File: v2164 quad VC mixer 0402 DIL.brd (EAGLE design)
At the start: 31.8 x 14 mm, 34 parts, among them IC1 TL072JD, Q1 BA854SW

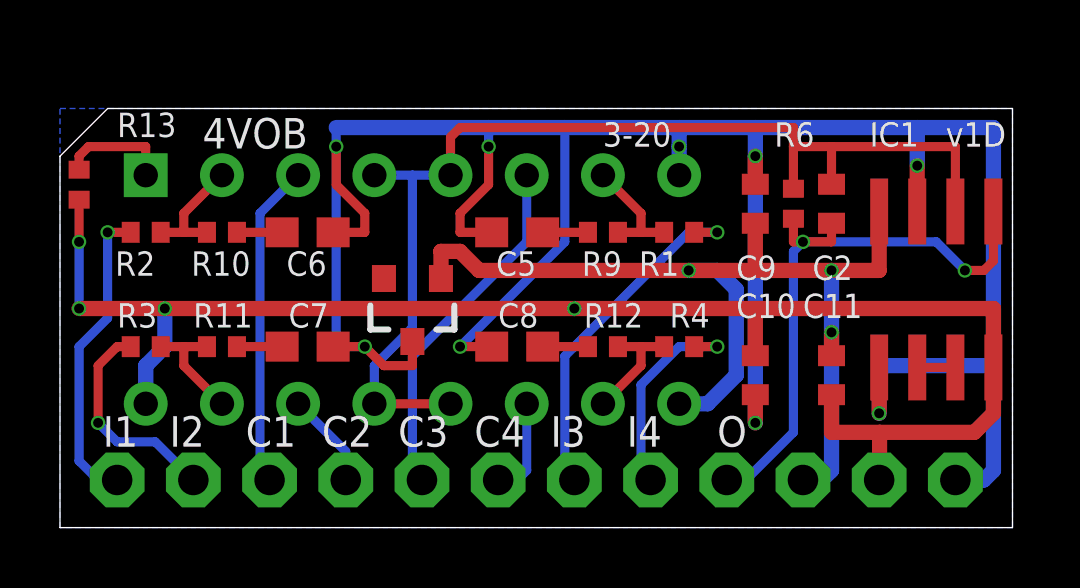
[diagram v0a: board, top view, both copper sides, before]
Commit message: Fixed some silk screen errors and replaced pads with some that solder slightly better
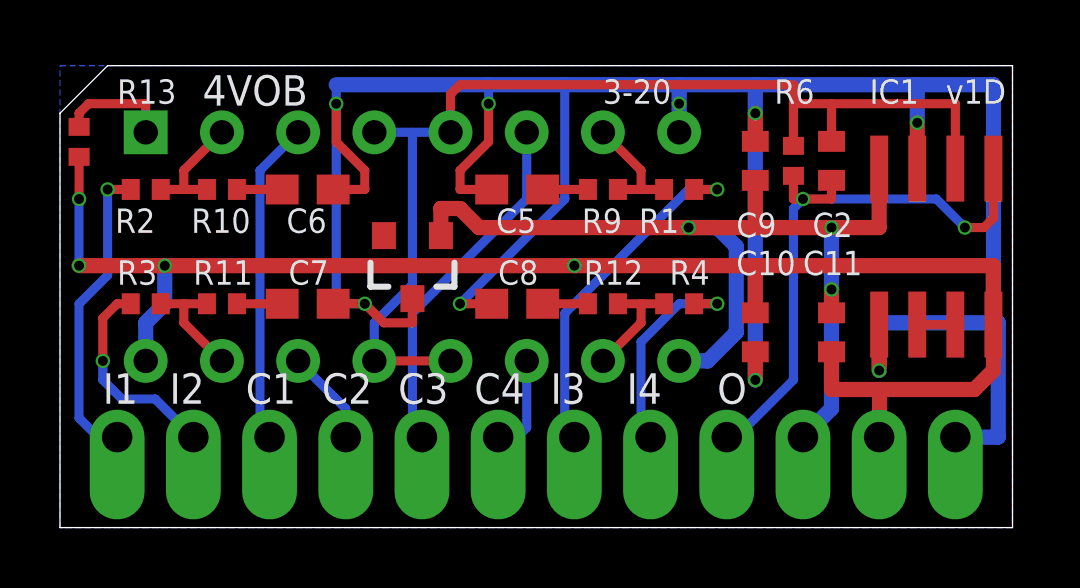
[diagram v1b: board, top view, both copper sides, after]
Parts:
- +15V, -15V, CV1, CV2, CV3, CV4, GND, IN1, IN2, IN3, IN4, OUT: device joakim:MA01N-1J -> joakim:SIP-PIN01-1J
- moved C2 1.43 mm to (26.0, 12.2)
- moved C5 1.43 mm to (15.6, 11.3)
- moved C6 1.43 mm to (8.57, 11.3)
- moved C9 1.43 mm to (23.5, 12.2)
- moved DA1 1.43 mm to (12.1, 9.37)
- moved IC1 1.43 mm to (29.5, 9.37)
- moved R1 1.43 mm to (21.0, 11.3)
- moved R10 1.43 mm to (5.71, 11.3)
- moved R13 1.43 mm to (0.95, 12.9)
- moved R2 1.43 mm to (3.17, 11.3)
- moved R6 1.43 mm to (24.8, 12.2)
- moved R9 1.43 mm to (18.4, 11.3)
- moved U$1 1.43 mm to (21.3, 7.52)
- moved +15V 1.43 mm to (27.6, 3.02), turned to 0 degrees
- moved -15V 1.43 mm to (25.1, 3.02), turned to 0 degrees
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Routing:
- net GND: track 88.8 -> 89.3 mm
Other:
- board size 31.8 x 14 mm -> 31.8 x 15.4 mm
- board text added: "4 ch mixer"
- board text added: "Mount socket on this side!"
- board text removed: "Quad exp VCA"

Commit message: Changed diode to B5817 (1n5817) as BAT854 is not available at JLCPCB
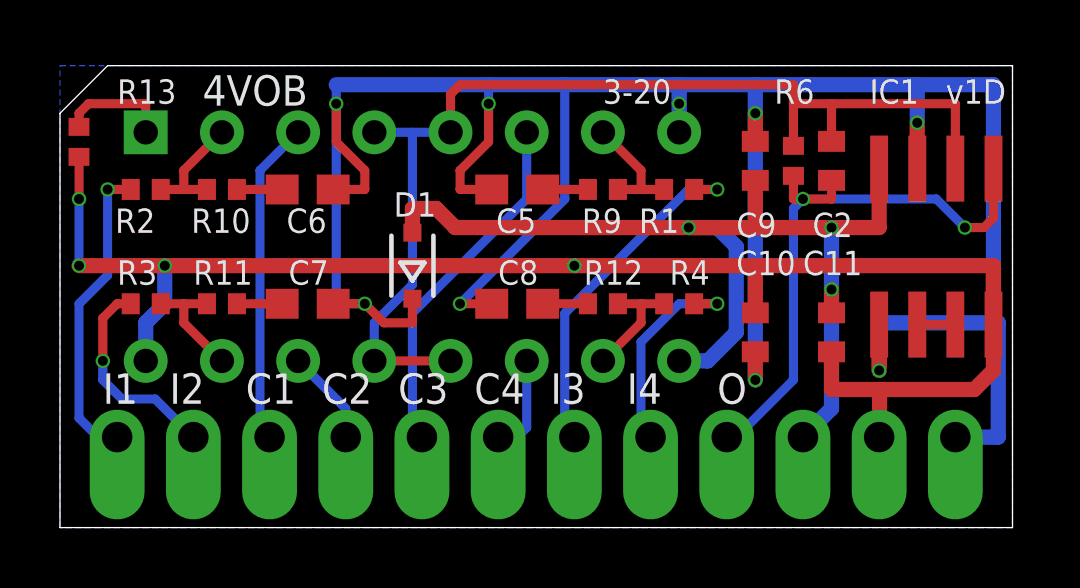
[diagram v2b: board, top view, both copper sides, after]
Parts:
- removed Q1: BA854SW, joakim:SOT23-3J
- added D1: (no value), diode:SOD323-R
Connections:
- net -15V: now also D1.A; no longer Q1.1
- net GND: now also D1.C; no longer Q1.3
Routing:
- net -15V: track 34.5 -> 35.3 mm
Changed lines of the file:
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@@
 <setting verticaltext="up"/>
 </settings>
-<grid distance="6.25" unitdist="mil" unit="mm" style="lines" multiple="1" display="yes" altdistance="5" altunitdist="mil" altunit="mil"/>
+<grid distance="6.25" unitdist="mil" unit="mil" style="lines" multiple="1" display="yes" altdistance="5" altunitdist="mil" altunit="mil"/>
 <layers>
-<layer number="1" name="Top" color="4" fill="1" visible="no" active="yes"/>
+<layer number="1" name="Top" color="4" fill="1" visible="yes" active="yes"/>
 <layer number="2" name="Route2" color="16" fill="1" visible="no" active="no"/>
 <layer number="15" name="Route15" color="23" fill="1" visible="no" active="no"/>
@@
 <layer number="19" name="Unrouted" color="6" fill="1" visible="yes" active="yes"/>
 <layer number="20" name="Dimension" color="24" fill="1" visible="yes" active="yes"/>
-<layer number="21" name="tPlace" color="7" fill="1" visible="no" active="yes"/>
+<layer number="21" name="tPlace" color="7" fill="1" visible="yes" active="yes"/>
 <layer number="22" name="bPlace" color="7" fill="1" visible="yes" active="yes"/>
-<layer number="23" name="tOrigins" color="15" fill="1" visible="no" active="yes"/>
+<layer number="23" name="tOrigins" color="15" fill="1" visible="yes" active="yes"/>
 <layer number="24" name="bOrigins" color="15" fill="1" visible="yes" active="yes"/>
-<layer number="25" name="tNames" color="7" fill="1" visible="no" active="yes"/>
+<layer number="25" name="tNames" color="7" fill="1" visible="yes" active="yes"/>
 <layer number="26" name="bNames" color="7" fill="1" visible="yes" active="yes"/>
 <layer number="27" name="tValues" color="7" fill="1" visible="no" active="yes"/>
@@
 <layer number="37" name="tTest" color="7" fill="1" visible="no" active="yes"/>
 <layer number="38" name="bTest" color="7" fill="1" visible="no" active="yes"/>
-<layer number="39" name="tKeepout" color="4" fill="11" visible="no" active="yes"/>
+<layer number="39" name="tKeepout" color="4" fill="11" visible="yes" active="yes"/>
 <layer number="40" name="bKeepout" color="1" fill="11" visible="yes" active="yes"/>
-<layer number="41" name="tRestrict" color="4" fill="10" visible="no" active="yes"/>
+<layer number="41" name="tRestrict" color="4" fill="10" visible="yes" active="yes"/>
 <layer number="42" name="bRestrict" color="1" fill="10" visible="yes" active="yes"/>
 <layer number="43" name="vRestrict" color="2" fill="10" visible="no" active="yes"/>
@@
 <layer number="49" name="Reference" color="7" fill="1" visible="no" active="yes"/>
 <layer number="50" name="dxf" color="7" fill="1" visible="no" active="no"/>
-<layer number="51" name="tDocu" color="7" fill="1" visible="no" active="yes"/>
+<layer number="51" name="tDocu" color="7" fill="1" visible="yes" active="yes"/>
 <layer number="52" name="bDocu" color="7" fill="1" visible="yes" active="yes"/>
 <layer number="53" name="tGND_GNDA" color="7" fill="9" visible="no" active="no"/>
@@
 <attribute name="VALUE" x="25.5905" y="11.27125" size="1.27" layer="27" rot="R270"/>
 </element>
-<element name="Q1" library="joakim" package="SOT23-3J" value="BA854SW" x="12.065" y="8.73125" smashed="yes" rot="R180">
-<attribute name="VALUE" x="13.081" y="8.92175" size="0.4064" layer="27" rot="R180"/>
-</element>
 <element name="U$1" library="joakim" package="XONIK_LOGO_18" value="" x="21.2725" y="7.51735" smashed="yes" rot="MR0"/>
+<element name="D1" library="diode" library_urn="urn:adsk.eagle:library:210" package="SOD323-R" package3d_urn="urn:adsk.eagle:package:43437/1" value="" x="12.065" y="8.73125" smashed="yes" rot="R90">
+<attribute name="NAME" x="11.44125" y="10.36625" size="0.8128" layer="25" font="vector"/>
+<attribute name="POPULARITY" value="4" x="12.065" y="8.73125" size="0.8128" layer="27" font="vector" rot="R90" display="off"/>
+<attribute name="VALUE" x="14.365" y="7.63125" size="1.27" layer="27" rot="R90"/>
+</element>
 </elements>
 <signals>
@@
 <wire x1="31.59125" y1="3.01625" x2="31.59125" y2="6.82625" width="0.508" layer="16"/>
 <wire x1="27.6225" y1="6.82625" x2="27.6225" y2="5.23875" width="0.508" layer="16"/>
-<contactref element="Q1" pad="3"/>
 <wire x1="9.4225" y1="11.27125" x2="10.4775" y2="11.27125" width="0.3048" layer="1"/>
 <wire x1="10.4775" y1="11.27125" x2="10.4775" y2="11.90625" width="0.3048" layer="1"/>
@@
 <wire x1="13.6525" y1="11.90625" x2="14.605" y2="12.85875" width="0.3048" layer="1"/>
 <via x="14.605" y="14.12875" extent="1-16" drill="0.3302"/>
-<wire x1="12.065" y1="7.63125" x2="12.065" y2="6.82625" width="0.3048" layer="1"/>
 <wire x1="12.065" y1="6.82625" x2="11.1125" y2="6.82625" width="0.3048" layer="1"/>
 <wire x1="11.1125" y1="6.82625" x2="10.4775" y2="7.46125" width="0.3048" layer="1"/>
 <wire x1="14.605" y1="12.85875" x2="14.605" y2="14.12875" width="0.3048" layer="1"/>
+<contactref element="D1" pad="C"/>
+<wire x1="12.065" y1="7.63125" x2="12.065" y2="6.82625" width="0.3048" layer="1"/>
 </signal>
 <signal name="N$9">
@@
 <wire x1="26.035" y1="10.00125" x2="23.495" y2="10.00125" width="0.508" layer="1"/>
 <wire x1="23.495" y1="10.00125" x2="21.2725" y2="10.00125" width="0.508" layer="1"/>
-<wire x1="21.2725" y1="10.00125" x2="14.2875" y2="10.00125" width="0.508" layer="1"/>
-<wire x1="14.2875" y1="10.00125" x2="13.6525" y2="10.63625" width="0.508" layer="1"/>
-<wire x1="13.6525" y1="10.63625" x2="13.0175" y2="10.63625" width="0.508" layer="1"/>
+<wire x1="21.2725" y1="10.00125" x2="13.49375" y2="10.00125" width="0.508" layer="1"/>
+<wire x1="13.49375" y1="10.00125" x2="12.85875" y2="10.63625" width="0.508" layer="1"/>
 <wire x1="21.2725" y1="10.00125" x2="22.225" y2="10.00125" width="0.508" layer="16"/>
 <wire x1="22.86" y1="9.36625" x2="22.225" y2="10.00125" width="0.508" layer="16"/>
@@
 <via x="21.2725" y="10.00125" extent="1-16" drill="0.3302"/>
 <wire x1="23.495" y1="11.57375" x2="23.495" y2="10.00125" width="0.508" layer="1"/>
-<contactref element="Q1" pad="1"/>
-<wire x1="13.015" y1="9.73125" x2="13.015" y2="10.63375" width="0.508" layer="1"/>
-<wire x1="13.015" y1="10.63375" x2="13.0175" y2="10.63625" width="0.508" layer="1"/>
 <wire x1="26.035" y1="3.96875" x2="25.0825" y2="3.01625" width="0.508" layer="16"/>
 <wire x1="26.035" y1="3.96875" x2="26.035" y2="7.9375" width="0.508" layer="16"/>
@@
 <wire x1="26.035" y1="10.00125" x2="26.035" y2="7.9375" width="0.508" layer="16"/>
 <via x="26.035" y="10.00125" extent="1-16" drill="0.3302"/>
+<contactref element="D1" pad="A"/>
+<wire x1="12.85875" y1="10.63625" x2="12.065" y2="10.63625" width="0.508" layer="1"/>
+<wire x1="12.065" y1="10.63625" x2="12.065" y2="9.83125" width="0.508" layer="1"/>
 </signal>
 <signal name="OUT4">
